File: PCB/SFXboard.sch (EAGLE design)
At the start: 25 parts, among them J1 AVR_SPI_PRG_6PTH, J2 TERMBLOCK4POS, J3 POWER_JACKPTH, Q1 16MHz, Q2 BSS138, Q3 BSS138, Q4 BSS138, U1 ATMEGA16U2-AU, X1 USBSMD

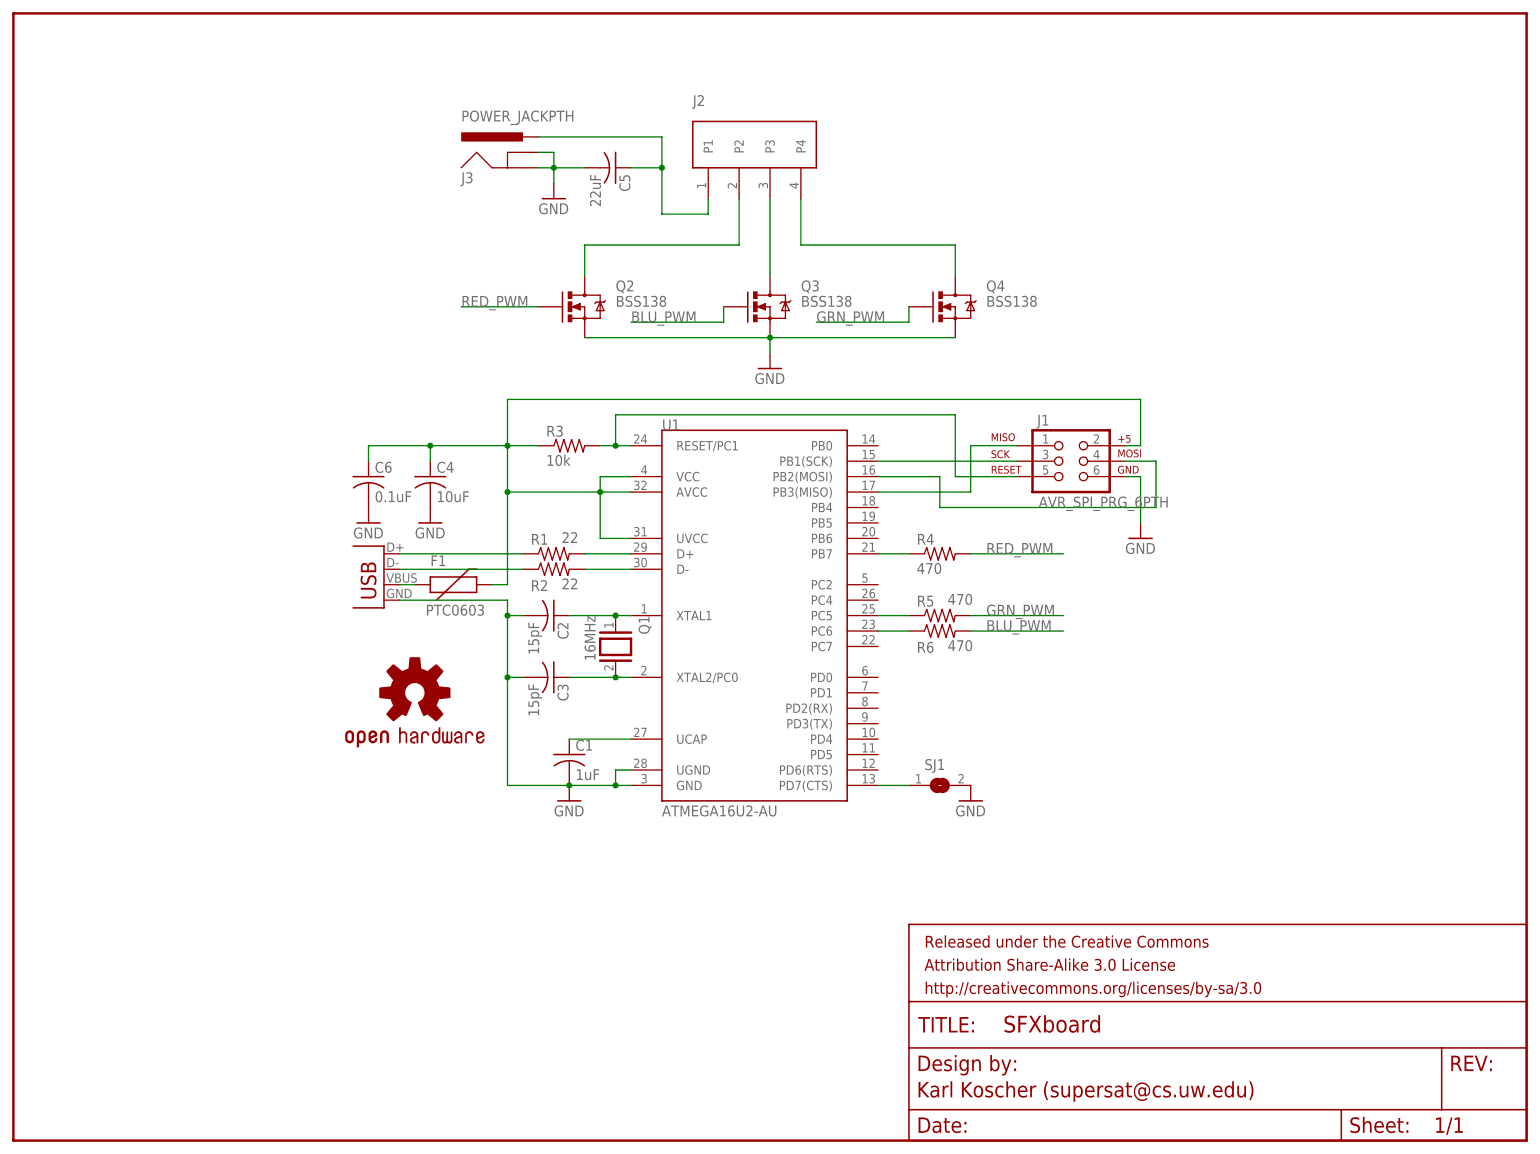
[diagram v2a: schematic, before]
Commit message: New board rev with all GPIO brought out
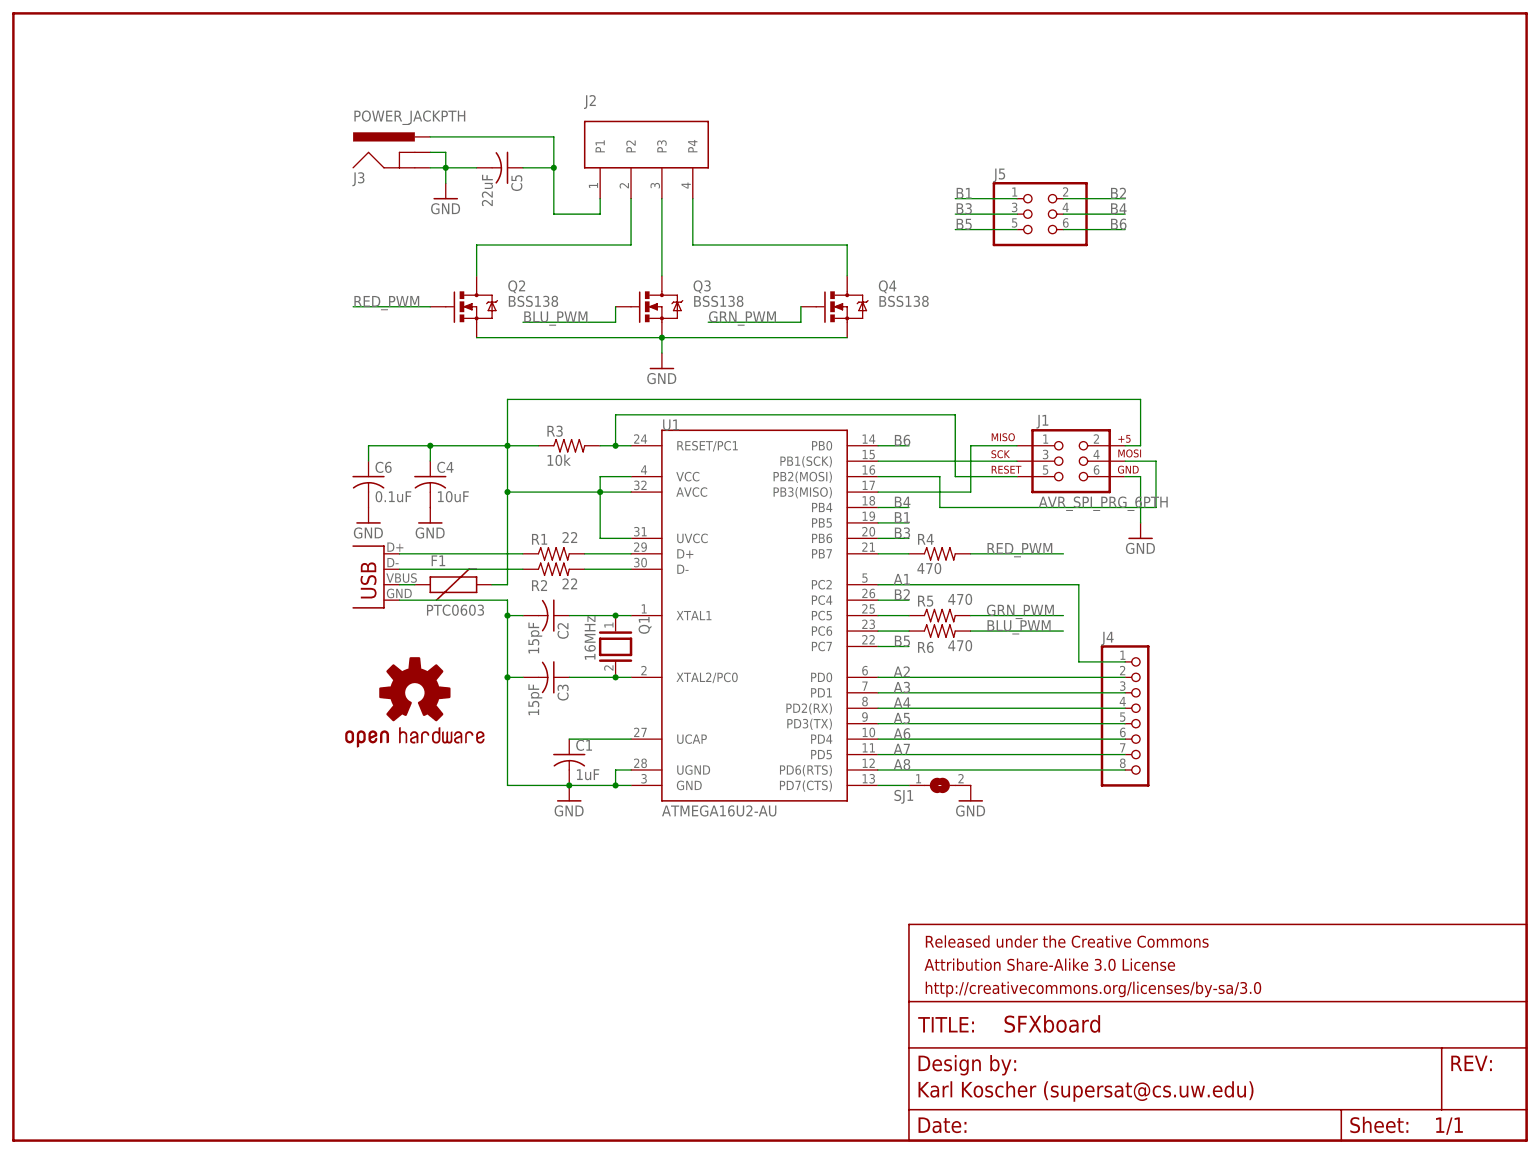
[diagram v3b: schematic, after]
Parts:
- added J4: (no value), pinhead:PINHD-1X8
- added J5: (no value), SparkFun-Connectors:PINHD-2X3
- C1, C2, C3: device resistor:C-USC0805 -> resistor:C-USC0603
- R1, R2, R3, R4, R5, R6: device resistor:R-US_R0805 -> resistor:R-US_R0603
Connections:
- new net A1: J4.1, U1.PC2
- new net A2: J4.2, U1.PD0
- new net A3: J4.3, U1.PD1
- new net A4: J4.4, U1.PD2(RX)
- new net A5: J4.5, U1.PD3(TX)
- new net A6: J4.6, U1.PD4
- new net A7: J4.7, U1.PD5
- new net A8: J4.8, U1.PD6(RTS)
- new net B1: J5.1, U1.PB5
- new net B2: J5.2, U1.PC4
- new net B3: J5.3, U1.PB6
- new net B4: J5.4, U1.PB4
- new net B5: J5.5, U1.PC7
- new net B6: J5.6, U1.PB0
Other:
- moved on the sheet: C5, J2, J3, Q2, Q3, Q4
